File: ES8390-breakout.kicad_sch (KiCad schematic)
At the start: 31 parts, among them J1 PJ-399B-6A, J3 Conn_01x02_Pin, J4 Conn_01x02_Pin, J5 PJ-399B-6A, U1 ES8390, U2 LP5907MFX-3.0, U3 MAX98306xDT

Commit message: schematics done?
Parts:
- removed C10, C12, C15: 1u, symbol Device:C_Small
- removed J1, J5: PJ-399B-6A, footprint_library:AUDIO-TH_PJ-399B-6A, symbol Project:PJ-399B-6A
- removed R4: 0, symbol Device:R
- removed R5: DNP, symbol Device:R
- removed U1: ES8390, Package_DFN_QFN:QFN-28-1EP_4x4mm_P0.45mm_EP2.6x2.6mm, symbol Project:ES8390
- added C18, C19, C20, C5, C8: 1u, Capacitor_SMD:C_0603_1608Metric, symbol Device:C_Small
- added CN1, CN2: PJ-327A, lcsc:AUDIO-SMD_XUNPU_PJ-327A, symbol LCSC:PJ-327A
- added J3, J4: AV-5, LCSC:CONN-TH_AV-5, symbol LCSC:AV-5
- added J5: Conn_01x14_Pin, Connector_PinHeader_2.54mm:PinHeader_1x14_P2.54mm_Vertical, symbol Connector:Conn_01x14_Pin
- added U3: ES8390, lcsc:QFN-28_L4.0-W4.0-P0.45-TL-EP2.7, symbol LCSC:ES8390
- added U4, U5: IM68A130AXTMA1, lcsc:MIC-SMD_4P-L3.4-W2.5_IM68A130V01, symbol LCSC:IM68A130AXTMA1
- C1: renamed from C8; footprint (none) -> Capacitor_SMD:C_0603_1608Metric; LCSC Part (none) -> C15849
- C10: renamed from C7; footprint (none) -> Capacitor_SMD:C_0603_1608Metric; LCSC Part (none) -> C15849
- C11, C13, C14, C16, C9: footprint (none) -> Capacitor_SMD:C_0603_1608Metric; LCSC Part (none) -> C15849
- C12: renamed from C2; footprint (none) -> Capacitor_SMD:C_0603_1608Metric; LCSC Part (none) -> C15849
- C15: renamed from C3; footprint (none) -> Capacitor_SMD:C_0603_1608Metric; LCSC Part (none) -> C15849
- C17: renamed from C6; footprint (none) -> Capacitor_SMD:C_0603_1608Metric; LCSC Part (none) -> C15849
- C2: renamed from C4; footprint (none) -> Capacitor_SMD:C_0603_1608Metric; LCSC Part (none) -> C15849
- C3: renamed from C1; footprint (none) -> Capacitor_SMD:C_0603_1608Metric; LCSC Part (none) -> C15849
- C4: renamed from C18; footprint (none) -> Capacitor_SMD:C_0603_1608Metric; LCSC Part (none) -> C96446
- C6: renamed from C5; footprint (none) -> Capacitor_SMD:C_0603_1608Metric; LCSC Part (none) -> C15849
- C7: renamed from C17; footprint (none) -> Capacitor_SMD:C_0603_1608Metric; LCSC Part (none) -> C15849
- FB1: value DNP -> BLM18BD421SN1D; footprint (none) -> Inductor_SMD:L_0603_1608Metric; LCSC Part (none) -> C113023
- J1: renamed from J3; footprint (none) -> Connector_JST:JST_XH_B2B-XH-A_1x02_P2.50mm_Vertical
- J2: renamed from J4; footprint (none) -> Connector_JST:JST_XH_B2B-XH-A_1x02_P2.50mm_Vertical
- R1: renamed from R7; footprint (none) -> Resistor_SMD:R_0603_1608Metric; LCSC Part (none) -> C95177
- R2: renamed from R3; footprint (none) -> Resistor_SMD:R_0603_1608Metric; LCSC Part (none) -> C95177
- R3: renamed from R6; footprint (none) -> Resistor_SMD:R_0603_1608Metric; LCSC Part (none) -> C95177
- U1: renamed from U2; LCSC Part (none) -> C2860052
- U2: renamed from U3; LCSC Part (none) -> C124549
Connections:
- net AD0/DMIC_SCL: now also J5.13 (Pin_13)
- net ADOUT/AD1: now also J5.10 (Pin_10), U3.8 (ASDOUT/AD1)
- net CCLK: now also J5.12 (Pin_12)
- net CDATA: now also J5.11 (Pin_11)
- net DSDIN: now also J5.9 (Pin_9), U3.6 (DSDIN)
- net GND: now also C13.2, C14.2, CN1.2, CN1.5, CN2.2, CN2.5, J3.1, J4.1, J5.14 (Pin_14), J5.3 (Pin_3), J5.5 (Pin_5), U3.18 (AGND), U3.29 (EP), U3.4 (DGND), U4.2 (GND), U4.4 (GND), U5.2 (GND), U5.4 (GND)
- net LIN1: now also C16.2, U4.1 (OUT); no longer C13.2
- net LIN2: now also C20.2, CN2.4
- net LOUTN: now also C8.1
- net LOUTP: now also C11.1, CN1.4, J3.2
- net LRCK: now also J5.8 (Pin_8), U3.7 (LRCK)
- net MCLK: now also J5.6 (Pin_6)
- net RIN1: now also C18.2, U5.1 (OUT); no longer C14.2
- net RIN2: now also C19.1, CN2.6; no longer C16.2
- net ROUTP: now also C5.1, CN1.6, J4.2; no longer C11.1
- net SCLK: now also J5.7 (Pin_7), U3.5 (SCLK)
- net VAMP: now also J5.1 (Pin_1)
- net VDDA: now also C13.1, C14.1, C17.1, FB1.2, U3.17 (AVDD), U4.3 (VDD), U5.3 (VDD)
- net VIO: now also J5.4 (Pin_4)
- net VLDO: now also J5.2 (Pin_2)
- net at C16.1: now also U3.24 (LIN1/DMIC_SDA)
- net at C9.2: now also U3.14 (ROUTN)
- net at C2.1, R1.1: now also U3.2 (DVDD)
- net at C11.2: now also U3.15 (LOUTP)
- net at C12.1: now also U3.19 (ADCVREF)
- net at C15.1: now also U3.20 (VMID)
- net at C3.1: now also U3.10 (DACVREF)
- net at C6.1, R3.1: now also U3.3 (PVDD)
- new net: C20.1, U3.22 (LIN2)
- new net: C5.2, U3.11 (ROUTP)
- new net: C8.2, U3.12 (LOUTN)
- new net: C19.2, U3.21 (RIN2)
- new net: C18.1, U3.23 (RIN1/DMIC_SCL)
- no-connect marks 0 -> 5
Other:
- company: (none) -> Maximilian Weber
- title: (none) -> ES8390 Breakout Board
- moved on the sheet: C1, C10, C12, C15, C17, C2, C3, C4, C6, C7, J1, J2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

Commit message: lib cleanup, start schematic
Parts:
- added H1, H2, H3, H4: MountingHole, MountingHole:MountingHole_3.2mm_M3_DIN965, symbol Mechanical:MountingHole
- C13, C14, C7: value 1u -> 100n; LCSC Part C15849 -> C14663
- CN1: renamed from J3; footprint LCSC:CONN-TH_AV-5 -> lcsc:CONN-TH_AV-5
- CN2: renamed from J4; footprint LCSC:CONN-TH_AV-5 -> lcsc:CONN-TH_AV-5
- renumbered J5 to CN3, CN1 to CN4, CN2 to CN5

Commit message: guitar input stage?
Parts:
- removed C14: 100n, Capacitor_SMD:C_0603_1608Metric, symbol Device:C_Small
- removed U5: IM68A130AXTMA1, lcsc:MIC-SMD_4P-L3.4-W2.5_IM68A130V01, symbol LCSC:IM68A130AXTMA1
- added J3: AudioJack2, symbol Connector_Audio:AudioJack2
- added U6: TLV9062, symbol Amplifier_Operational:TLV9062
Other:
- moved on the sheet: C13, CN3, CN5, U4

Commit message: guitar input stage schematic
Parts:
- added C14: 100p, Capacitor_SMD:C_0603_1608Metric, symbol Device:C_Small
- added C21, C22: 100n, Capacitor_SMD:C_0603_1608Metric, symbol Device:C_Small
- added R10, R11, R8, R9: 100k, Resistor_SMD:R_0603_1608Metric, symbol Device:R
- added R5, R6: 1M, Resistor_SMD:R_0603_1608Metric, symbol Device:R
- added R7: 4k7, Resistor_SMD:R_0603_1608Metric, symbol Device:R
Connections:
- net GND: now also J3.S, U6.4 (V-), C14.2, C22.2, R5.2, R6.2, R9.2
- net RIN1: now also U6.7, R10.1, R11.2
- net VDDA: now also U6.8 (V+), C22.1, R8.1
- net VBIAS: now reaches U6.1
- net VBIAS: now also U6.2 (-), R11.1
- net at U6.3 (+): now also R8.2, R9.1
- net at U6.5 (+): now also C14.1, R7.2
- net at U6.6 (-): now also R10.2
- net at J3.T: now also C21.1, R5.1
- new net: C21.2, R6.1, R7.1
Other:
- moved on the sheet: C1, C10, C13, C4, C7, FB1, J1, J2, J3, R2, U1, U2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

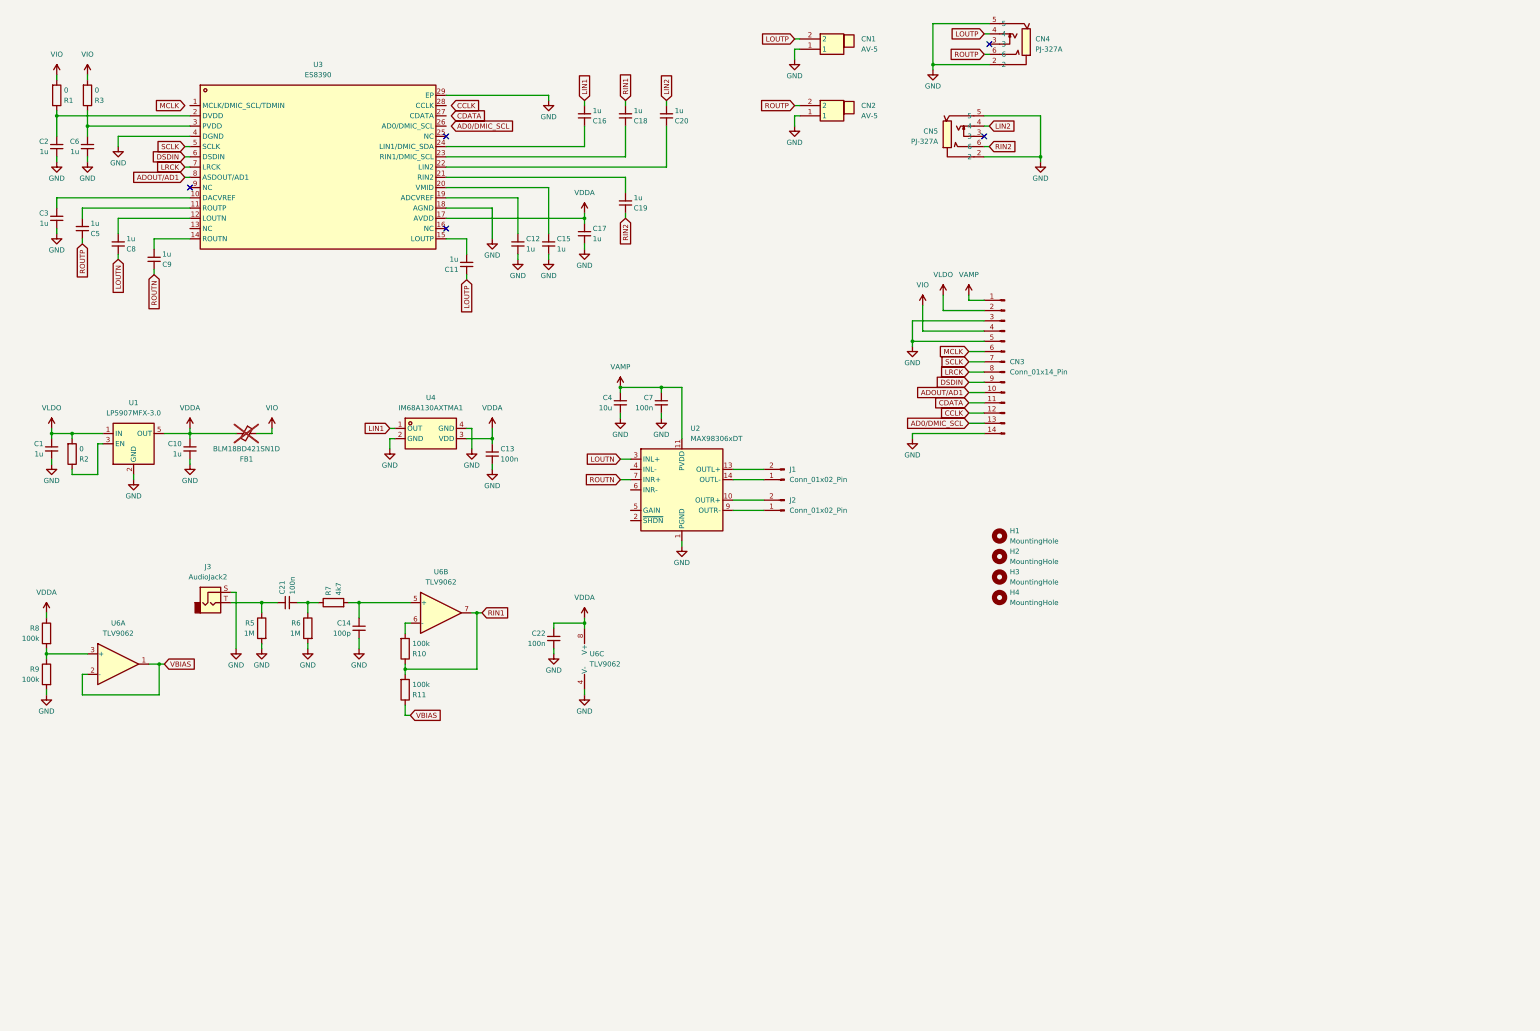
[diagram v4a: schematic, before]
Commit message: add ESD
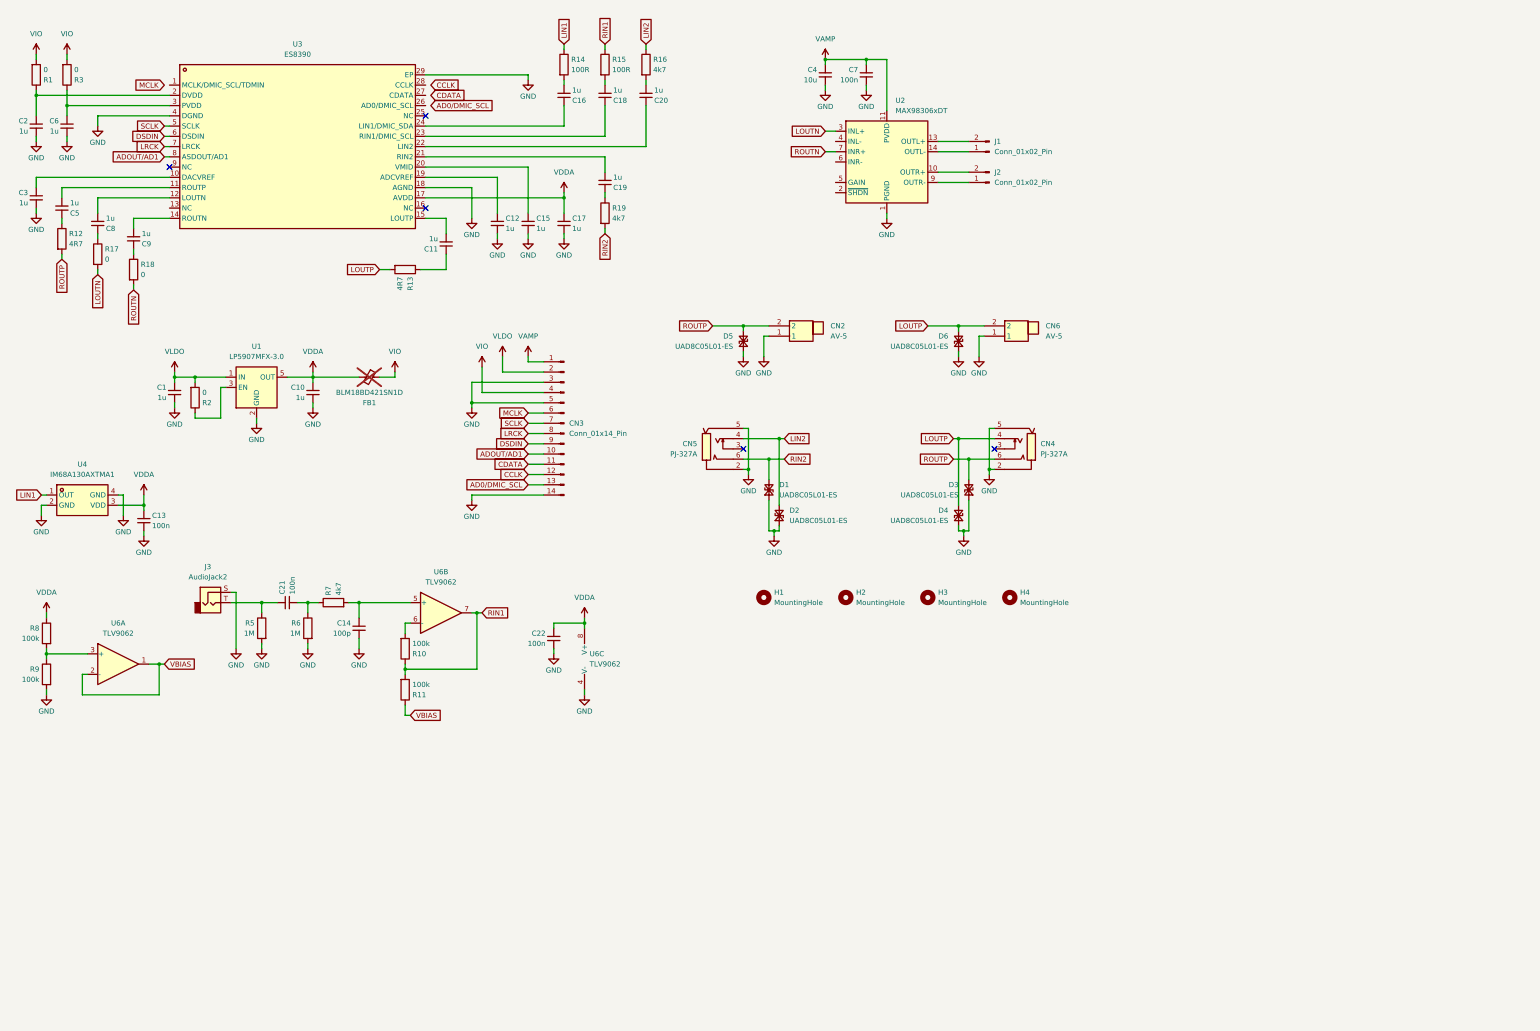
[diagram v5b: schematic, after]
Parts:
- removed CN1: AV-5, lcsc:CONN-TH_AV-5, symbol LCSC:AV-5
- added CN6: AV-5, lcsc:CONN-TH_AV-5, symbol LCSC:AV-5
- added D1, D2, D3, D4, D5, D6: UAD8C05L01-ES, symbol Device:D_TVS_Small
- added R12, R13: 4R7, Resistor_SMD:R_0603_1608Metric, symbol Device:R
- added R14, R15: 100R, Resistor_SMD:R_0603_1608Metric, symbol Device:R
- added R16, R19: 4k7, Resistor_SMD:R_0603_1608Metric, symbol Device:R
- added R17, R18: 0, Resistor_SMD:R_0603_1608Metric, symbol Device:R
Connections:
- net GND: now also CN6.1, D1.1 (A1), D2.1 (A1), D3.1 (A1), D4.1 (A1), D5.1 (A1), D6.1 (A1)
- net LIN1: now also R14.1; no longer C16.2
- net LIN2: now also D2.2 (A2), R16.1; no longer C20.2
- net LOUTN: now also R17.2; no longer C8.1
- net LOUTP: now also CN6.2, D4.2 (A2), D6.2 (A2), R13.2; no longer C11.1
- net RIN1: now also R15.1; no longer C18.2
- net RIN2: now also D1.2 (A2), R19.2; no longer C19.1
- net ROUTN: now also R18.2; no longer C9.1
- net ROUTP: now also D3.2 (A2), D5.2 (A2), R12.2; no longer C5.1
- new net: C9.1, R18.1
- new net: C8.1, R17.1
- new net: C16.2, R14.2
- new net: C20.2, R16.2
- new net: C11.1, R13.1
- new net: C19.1, R19.1
- new net: C5.1, R12.1
- new net: C18.2, R15.2
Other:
- moved on the sheet: C1, C10, C11, C12, C13, C15, C16, C17, C18, C19, C2, C20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

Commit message: fix guitar input stage
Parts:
- added C23: 100p, Capacitor_SMD:C_0603_1608Metric, symbol Device:C_Small
- R10, R11: value 100k -> 10k
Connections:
- net GND: now also C23.2; no longer C14.2, R6.2
- net RIN1: now also R10.2; no longer R10.1, R11.2
- net VBIAS: now also C14.2, R6.2, C23.1
- net at U6.6 (-): now also R10.1, R11.2; no longer R10.2
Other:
- moved on the sheet: C1, C10, C13, C14, C21, C22, C4, C7, CN3, FB1, J1, J2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

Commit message: add lcsc parts, ts-mono jack
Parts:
- removed J3: AudioJack2, symbol Connector_Audio:AudioJack2
- added J1: PJ-603A, lcsc:AUDIO-TH_PJ-603A, symbol LCSC:PJ-603A
- C1: renamed from C2; now left out of the parts list
- C12: renamed from C11; now left out of the parts list
- C13: renamed from C12; now left out of the parts list
- C15, C16, C17, C18, C19, C20: now left out of the parts list
- C2: renamed from C3; now left out of the parts list
- C3: renamed from C5; now left out of the parts list
- C4: renamed from C6; now left out of the parts list
- C5: renamed from C1; now left out of the parts list
- C6: renamed from C8; now left out of the parts list
- C7: renamed from C9; now left out of the parts list
- C9: renamed from C10; now left out of the parts list
- D1: renamed from D5; footprint (none) -> Diode_SMD:D_SOD-882
- D2: renamed from D1; footprint (none) -> Diode_SMD:D_SOD-882
- D3: renamed from D2; footprint (none) -> Diode_SMD:D_SOD-882
- D4: renamed from D6; footprint (none) -> Diode_SMD:D_SOD-882
- D5: renamed from D4; footprint (none) -> Diode_SMD:D_SOD-882
- D6: renamed from D3; footprint (none) -> Diode_SMD:D_SOD-882
- R10: renamed from R6; LCSC Part C95177 -> C105578
- R11: renamed from R7; LCSC Part C95177 -> C99782
- R12: renamed from R11; LCSC Part C95177 -> C98220
- R13: renamed from R10; LCSC Part C95177 -> C98220
- R14: renamed from R13; LCSC Part C95177 -> C105588
- R15: renamed from R14; LCSC Part C95177 -> C105588
- R16: renamed from R15; LCSC Part C95177 -> C105588
- R17: renamed from R19; LCSC Part C95177 -> C99782
- R18: renamed from R16; LCSC Part C95177 -> C99782
- R2: renamed from R8; LCSC Part C95177 -> C14675
- R3: renamed from R9; LCSC Part C95177 -> C14675
- R4: renamed from R12; LCSC Part C95177 -> C105588
- R9: renamed from R5; LCSC Part C95177 -> C105578
- U1: renamed from U6; footprint (none) -> lcsc:SOIC-8_L5.0-W4.0-P1.27-LS6.0-BL; LCSC Part (none) -> C54539963
- renumbered C21 to C10, C14 to C11, C22 to C14, C13 to C21, C4 to C22, C7 to C23, C23 to C8, CN3 to CN1, CN5 to CN2, CN2 to CN3, CN6 to CN4, CN4 to CN5, J1 to J2, J2 to J3, R3 to R5, R2 to R6, R17 to R7, R18 to R8, U1 to U2, U2 to U5
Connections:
- net GND: now also J1.2
- net at C10.1, R9.1: now also J1.5
- no-connect marks 5 -> 7

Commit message: continue layout
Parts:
- removed CN3, CN4: AV-5, lcsc:CONN-TH_AV-5, symbol LCSC:AV-5
- removed D1, D4: UAD8C05L01-ES, Diode_SMD:D_SOD-882, symbol Device:D_TVS_Small
- added C21, C22: 1u, Capacitor_SMD:C_0603_1608Metric, symbol Device:C_Small
- added R19, R20: 0, Resistor_SMD:R_0603_1608Metric, symbol Device:R
- U3: footprint lcsc:QFN-28_L4.0-W4.0-P0.45-TL-EP2.7 -> Package_DFN_QFN:QFN-28-1EP_4x4mm_P0.45mm_EP2.6x2.6mm
- renumbered C22 to C23, C23 to C24, C21 to C25, CN5 to CN3, D2 to D1, D3 to D2, D5 to D3, D6 to D4
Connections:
- net AD0/DMIC_SCL: now also U3.26 (AD0/DMIC_SCL)
- net CCLK: now also U3.28 (CCLK)
- net CDATA: now also U3.27 (CDATA)
- net GND: now also CN1.1 (Pin_1), C21.2, C22.2, R20.1; no longer CN1.3 (Pin_3), CN1.5 (Pin_5)
- net LIN1: now also R13.2, U1.7; no longer U4.1 (OUT)
- net RIN1: now also U4.1 (OUT); no longer R13.2, U1.7
- net VAMP: now also CN1.2 (Pin_2), R19.2; no longer CN1.1 (Pin_1)
- net VLDO: now also CN1.3 (Pin_3); no longer CN1.2 (Pin_2)
- net AMP_SHDN: now reaches U5.2 (~{SHDN})
- net AMP_SHDN: now also CN1.5 (Pin_5)
- net at U5.4 (INL-): now also C21.1
- net at U5.5 (GAIN): now also R19.1, R20.2
- net at U5.6 (INR-): now also C22.1
- no-connect marks 7 -> 8
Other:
- moved on the sheet: C25, U4
